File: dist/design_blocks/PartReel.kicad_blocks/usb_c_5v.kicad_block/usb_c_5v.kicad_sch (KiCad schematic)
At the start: 3 parts, among them J1 USB-C 16P

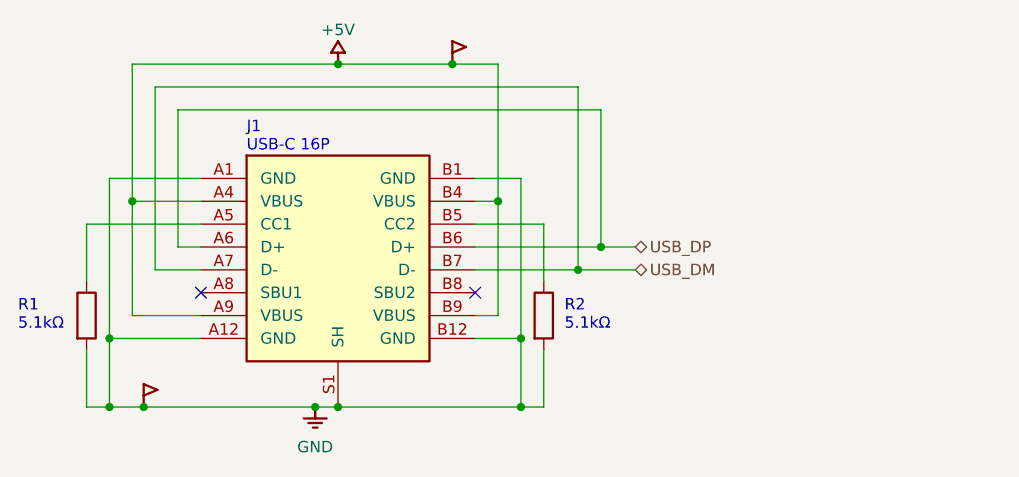
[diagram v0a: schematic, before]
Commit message: 디자인 블록 배포물 갱신 (usb_c_5v v0.2 ESD 포함, boardworks 빌드)
Co-Authored-By: Claude Fable 5 <noreply@anthropic.com>
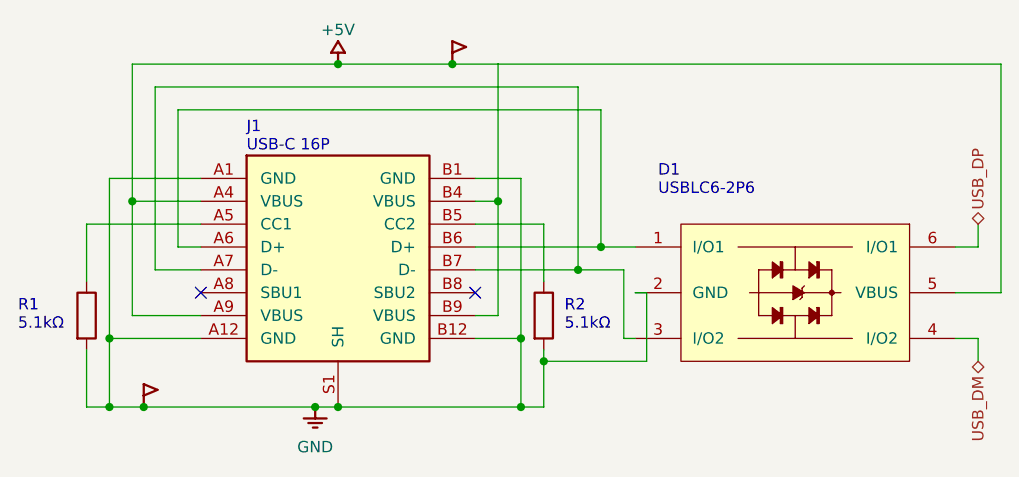
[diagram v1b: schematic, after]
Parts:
- added D1: USBLC6-2P6, PCM_PartReel:cern_usblc6_2p6, symbol PartReel:USBLC6-2
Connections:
- net +5V: now also D1.5 (VBUS)
- net GND: now also D1.2 (GND)
- net USB_DM: now also D1.4 (I/O2); no longer J1.A7 (D-), J1.B7 (D-)
- net USB_DP: now also D1.6 (I/O1); no longer J1.A6 (D+), J1.B6 (D+)
- new net: D1.1 (I/O1), J1.A6 (D+), J1.B6 (D+)
- new net: D1.3 (I/O2), J1.A7 (D-), J1.B7 (D-)
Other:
- note added: "D1"
- note added: "USBLC6-2P6"
